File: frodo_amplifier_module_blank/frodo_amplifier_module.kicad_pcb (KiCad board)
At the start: 2 copper layers, 16.5 x 10 mm, 19 parts, among them IC1 INA826AID, IC2 AS321KTR-G1, J1 Conn_01x01_Socket, J2 Conn_01x01_Socket, J3 Conn_01x01_Socket, J4 Conn_01x01_Socket, J5 Conn_01x01_Socket, J6 Conn_01x01_Socket, J7 Conn_01x01_Socket, J8 Conn_01x01_Socket

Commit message: fixed my messup
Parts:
- moved JP1 0.34 mm to (85.2, 54.0), turned to 90 degrees
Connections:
- IC2 pad 3: ref -> Net-(IC2-INPUT_-)
- IC2 pad 4: ref -> Net-(IC2-INPUT_-)
- JP1 pad 2: Net-(IC2-INPUT_+) -> ref
- JP1 pad 3: Net-(JP1-B) -> Net-(IC2-INPUT_-)
- R3 pad 1: Net-(JP1-B) -> Net-(IC2-INPUT_+)
- R4 pad 2: Net-(JP1-B) -> Net-(IC2-INPUT_+)
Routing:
- net Net-(JP1-B): track 5.22 -> 0.00 mm, vias 1 -> 0
- net Net-(IC2-INPUT_-): track 0.00 -> 3.40 mm, vias 0 -> 1
- net ref: track 7.22 -> 8.35 mm
- net Net-(IC2-INPUT_+): track 2.09 -> 3.02 mm, vias 1 -> 0

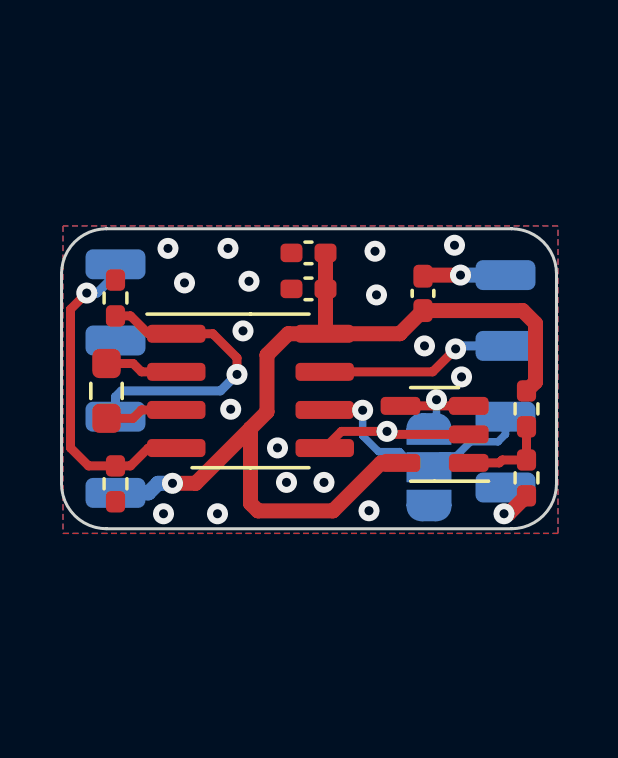
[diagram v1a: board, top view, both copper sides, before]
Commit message: updated mounting holes and footprints of c2 and fb1
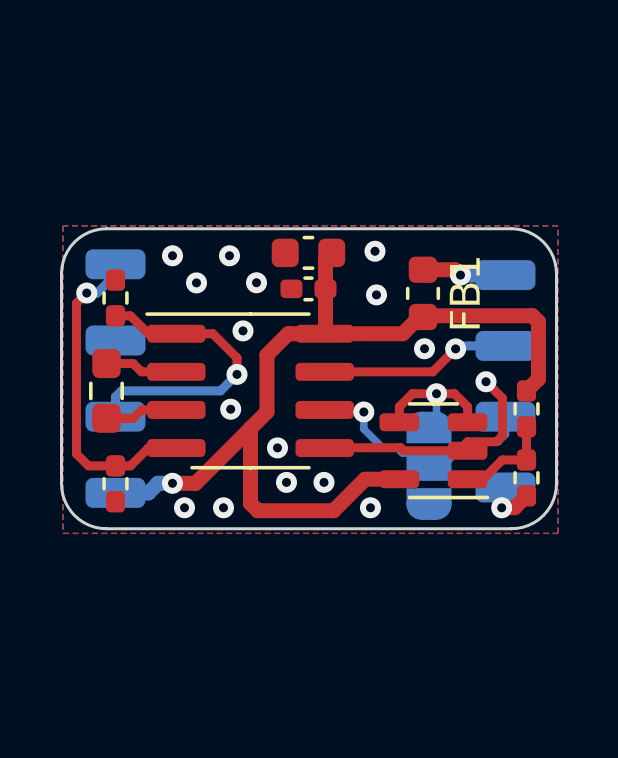
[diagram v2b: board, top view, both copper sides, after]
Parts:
- C2: footprint Capacitor_SMD:C_0402_1005Metric_Pad0.74x0.62mm_HandSolder -> Capacitor_SMD:C_0603_1608Metric
- FB1: footprint Inductor_SMD:L_0402_1005Metric_Pad0.77x0.64mm_HandSolder -> Inductor_SMD:L_0603_1608Metric
- moved IC2 0.55 mm to (85.4, 53.4)
- moved JP1 0.05 mm to (85.2, 53.9)
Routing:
- net GND: track 6.07 -> 9.37 mm, vias 19 -> 17
- net Net-(IC2-INPUT_-): track 3.40 -> 4.99 mm
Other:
- board text added: "1-> gnd 3-> ref"
- board text removed: "1 for gnd 3 for ref"

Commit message: changed mounting holes
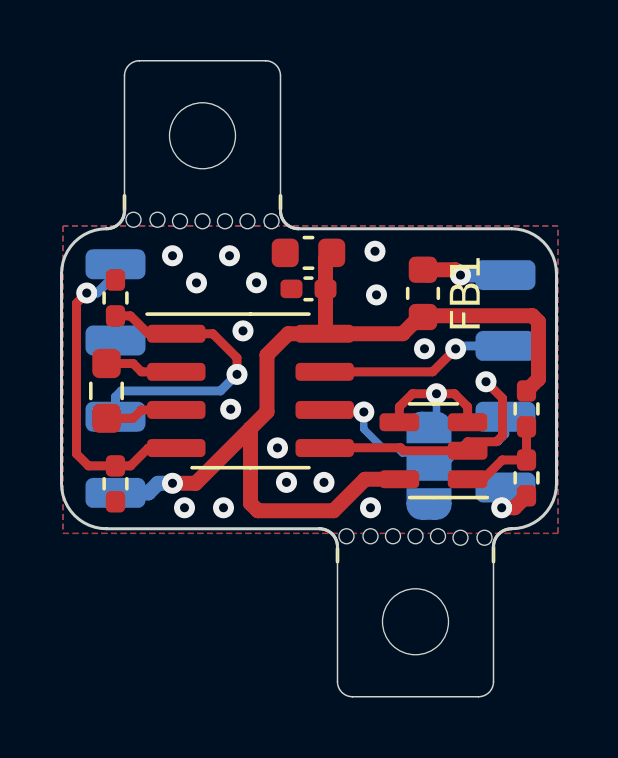
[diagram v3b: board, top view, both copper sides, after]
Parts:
- added REF**: MountingHole_2.2mm_M2, MountingHole:MountingHole_2.2mm_M2, F.Cu at (84.8, 59.1)
- added REF**: MountingHole_2.2mm_M2, MountingHole:MountingHole_2.2mm_M2, F.Cu at (77.7, 42.9)
- added mouse-bite-2mm-slot: VAL**, MountingEquipment:mouse-bite-2mm-slot, F.Cu at (84.9, 57.0)
- added mouse-bite-2mm-slot: VAL**, MountingEquipment:mouse-bite-2mm-slot, F.Cu at (77.6, 45.0)
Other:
- board size 16.5 x 10 mm -> 16.5 x 21.2 mm
- board text added: "1 gnd"
- board text added: "3 ref"
- board text added: "JLCJLCJLCJLC"
- board text removed: "1-> gnd 3-> ref"
